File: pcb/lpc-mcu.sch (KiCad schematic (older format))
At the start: 6 parts, among them CON1 ARM-SWD-HEADER, IC1 LPC11U14FBD48

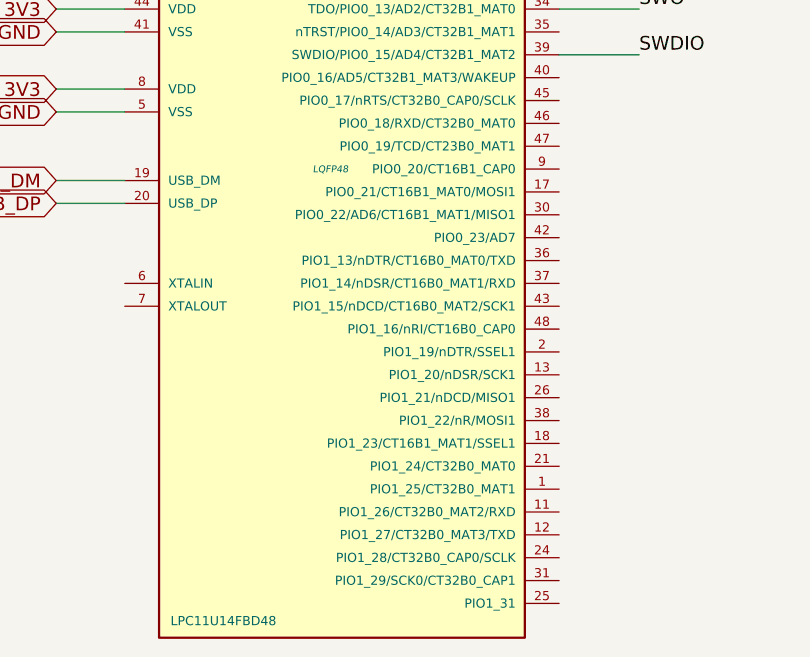
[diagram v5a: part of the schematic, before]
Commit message: made a footprint for the lpc11u14 that should be nice to hand solder
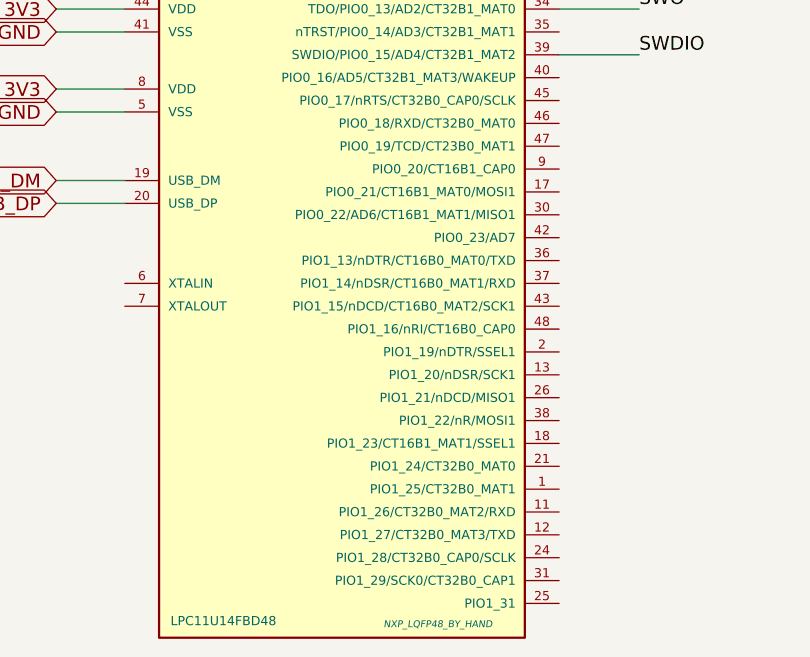
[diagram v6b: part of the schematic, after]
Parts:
- IC1: footprint LQFP48 -> NXP_LQFP48_BY_HAND
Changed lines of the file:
@@
 Sheet 2 6
 Title ""
-Date "26 dec 2014"
+Date "27 dec 2014"
 Rev ""
 Comp ""
@@
 F 0 "IC1" H 4500 6250 40  0000 L BNN
 F 1 "LPC11U14FBD48" H 4550 2200 40  0000 L BNN
-F 2 "LQFP48" H 5250 4200 30  0000 C CIN
+F 2 "NXP_LQFP48_BY_HAND" H 5720 2210 30  0000 C CIN
 F 3 "~" H 5250 4200 60  0000 C CNN
 	1    5250 4200

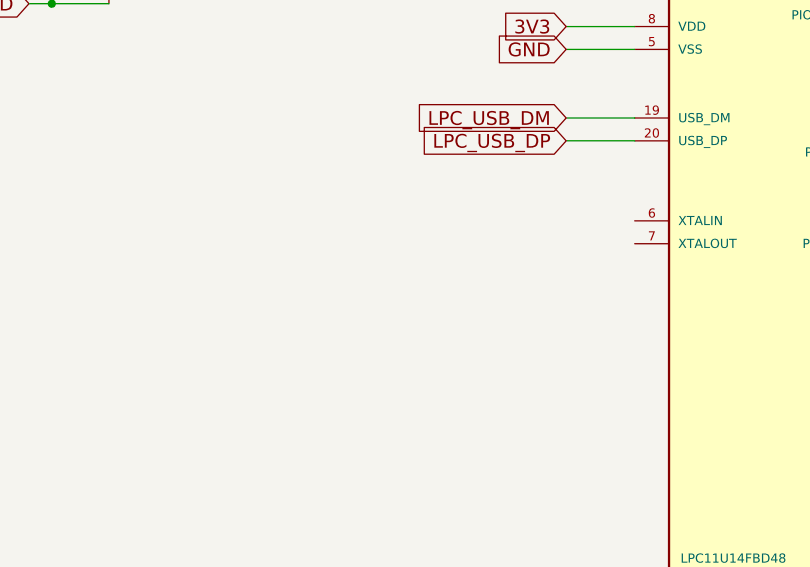
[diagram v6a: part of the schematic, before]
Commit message: pulled in regulator footprint, started on pcb
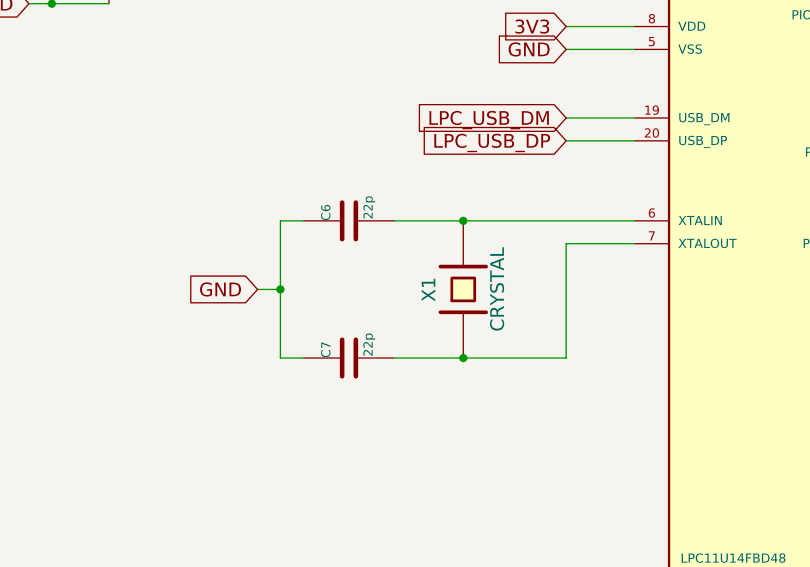
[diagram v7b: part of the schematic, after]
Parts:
- added C6, C7: 22p, ~, symbol C
- added X1: CRYSTAL, ~, symbol CRYSTAL
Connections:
- net GND: now also C6.1, C7.1
- net at IC1.6 (XTALIN): now also C6.2, X1.2
- net at IC1.7 (XTALOUT): now also C7.2, X1.1
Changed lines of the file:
@@
 Text Notes 8100 2500 0    60   ~ 0
 TO DO: figure out if we need to reduce the USB\nbus voltage before it gets to the MCU.
+$Comp
+L CRYSTAL X1
+U 1 1 549E7192
+P 3600 5000
+F 0 "X1" H 3600 5150 60  0000 C CNN
+F 1 "CRYSTAL" H 3600 4850 60  0000 C CNN
+F 2 "~" H 3600 5000 60  0000 C CNN
+F 3 "~" H 3600 5000 60  0000 C CNN
+	1    3600 5000
+	0    -1   -1   0
+$EndComp
+$Comp
+L C C6
+U 1 1 549E71AB
+P 3100 4700
+F 0 "C6" H 3100 4800 40  0000 L CNN
+F 1 "22p" H 3106 4615 40  0000 L CNN
+F 2 "~" H 3138 4550 30  0000 C CNN
+F 3 "~" H 3100 4700 60  0000 C CNN
+	1    3100 4700
+	0    -1   -1   0
+$EndComp
+$Comp
+L C C7
+U 1 1 549E71C4
+P 3100 5300
+F 0 "C7" H 3100 5400 40  0000 L CNN
+F 1 "22p" H 3106 5215 40  0000 L CNN
+F 2 "~" H 3138 5150 30  0000 C CNN
+F 3 "~" H 3100 5300 60  0000 C CNN
+	1    3100 5300
+	0    -1   -1   0
+$EndComp
+Text GLabel 2700 5000 0    60   Input ~ 0
+GND
+Wire Wire Line
+	2900 4700 2800 4700
+Wire Wire Line
+	2800 4700 2800 5300
+Wire Wire Line
+	2800 5300 2900 5300
+Wire Wire Line
+	2700 5000 2800 5000
+Connection ~ 2800 5000
+Wire Wire Line
+	3300 5300 4050 5300
+Wire Wire Line
+	3300 4700 4350 4700
+Connection ~ 3600 4700
+Wire Wire Line
+	4050 5300 4050 4800
+Wire Wire Line
+	4050 4800 4350 4800
+Connection ~ 3600 5300
 $EndSCHEMATC

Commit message: power and usb - a bit more progress
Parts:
- added P4: GPIO, symbol CONN_6
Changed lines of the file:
@@
 	4050 4800 4350 4800
 Connection ~ 3600 5300
+$Comp
+L CONN_6 P4
+U 1 1 549E7D82
+P 9550 6000
+F 0 "P4" V 9500 6000 60  0000 C CNN
+F 1 "GPIO" V 9600 6000 60  0000 C CNN
+F 2 "" H 9550 6000 60  0000 C CNN
+F 3 "" H 9550 6000 60  0000 C CNN
+	1    9550 6000
+	1    0    0    -1
+$EndComp
 $EndSCHEMATC
